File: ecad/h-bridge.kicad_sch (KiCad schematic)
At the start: 9 parts, among them Q1 40N06D, Q2 40N06D, U1 IR2104

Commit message: Use IRS2104
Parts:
- removed C2: C, symbol Device:C_Polarized
- added C2: C, Capacitor_SMD:C_0603_1608Metric, symbol Device:C
- D1: value D -> ES1D; footprint (none) -> Diode_SMD:D_SMA; LCSC Part # (none) -> C82648
- Q1, Q2: footprint Package_DFN_QFN:PQFN-8-EP_6x5mm_P1.27mm_Generic -> Package_TO_SOT_SMD:PQFN_8x8
- R1, R2: footprint (none) -> Resistor_SMD:R_0603_1608Metric
- U1: footprint (none) -> Package_SO:SOIC-8_3.9x4.9mm_P1.27mm
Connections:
- net OUT: now also C2.2
- net at D1.1 (K), U1.8 (VB): now also C2.1
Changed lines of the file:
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@@
 			)
 		)
-		(property "Footprint" ""
+		(property "Footprint" "Resistor_SMD:R_0603_1608Metric"
 			(at 153.67 108.458 90)
 			(effects
@@
 			)
 		)
-		(property "Footprint" "Package_DFN_QFN:PQFN-8-EP_6x5mm_P1.27mm_Generic"
+		(property "Footprint" "Package_TO_SOT_SMD:PQFN_8x8"
 			(at 170.18 91.44 0)
 			(effects
@@
 			)
 		)
-		(property "Footprint" "Package_DFN_QFN:PQFN-8-EP_6x5mm_P1.27mm_Generic"
+		(property "Footprint" "Package_TO_SOT_SMD:PQFN_8x8"
 			(at 170.18 104.14 0)
 			(effects
@@
 			)
 		)
-		(property "Footprint" ""
+		(property "Footprint" "Resistor_SMD:R_0603_1608Metric"
 			(at 153.67 95.758 90)
 			(effects
@@
 			)
 		)
-		(property "Footprint" ""
+		(property "Footprint" "Package_SO:SOIC-8_3.9x4.9mm_P1.27mm"
 			(at 121.92 99.06 0)
 			(effects
@@
 				(path "/192016dd-1af9-4f75-bd76-63c005f8be5e/9897782e-08fe-4e99-a389-7b164bfce6c4"
 					(reference "U1")
-					(unit 1)
-				)
-			)
-		)
-	)
-	(symbol
-		(lib_id "Device:C_Polarized")
-		(at 135.89 99.06 0)
-		(unit 1)
-		(exclude_from_sim no)
-		(in_bom yes)
-		(on_board yes)
-		(dnp no)
-		(fields_autoplaced yes)
-		(property "Reference" "C2"
-			(at 139.7 96.9009 0)
-			(effects
-				(font
-					(size 1.27 1.27)
-				)
-				(justify left)
-			)
-		)
-		(property "Value" "C"
-			(at 139.7 99.4409 0)
-			(effects
-				(font
-					(size 1.27 1.27)
-				)
-				(justify left)
-			)
-		)
-		(property "Footprint" ""
-			(at 136.8552 102.87 0)
-			(effects
-				(font
-					(size 1.27 1.27)
-				)
-				(hide yes)
-			)
-		)
-		(property "Datasheet" "~"
-			(at 135.89 99.06 0)
-			(effects
-				(font
-					(size 1.27 1.27)
-				)
-				(hide yes)
-			)
-		)
-		(property "Description" "Polarized capacitor"
-			(at 135.89 99.06 0)
-			(effects
-				(font
-					(size 1.27 1.27)
-				)
-				(hide yes)
-			)
-		)
-		(pin "2"
-		)
-		(pin "1"
-		)
-		(instances
-			(project ""
-				(path "/192016dd-1af9-4f75-bd76-63c005f8be5e/9897782e-08fe-4e99-a389-7b164bfce6c4"
-					(reference "C2")
 					(unit 1)
 				)
@@
 	)
 	(symbol
+		(lib_id "Device:C")
+		(at 135.89 99.06 0)
+		(unit 1)
+		(exclude_from_sim no)
+		(in_bom yes)
+		(on_board yes)
+		(dnp no)
+		(fields_autoplaced yes)
+		(property "Reference" "C2"
+			(at 139.7 97.7899 0)
+			(effects
+				(font
+					(size 1.27 1.27)
+				)
+				(justify left)
+			)
+		)
+		(property "Value" "C"
+			(at 139.7 100.3299 0)
+			(effects
+				(font
+					(size 1.27 1.27)
+				)
+				(justify left)
+			)
+		)
+		(property "Footprint" "Capacitor_SMD:C_0603_1608Metric"
+			(at 136.8552 102.87 0)
+			(effects
+				(font
+					(size 1.27 1.27)
+				)
+				(hide yes)
+			)
+		)
+		(property "Datasheet" "~"
+			(at 135.89 99.06 0)
+			(effects
+				(font
+					(size 1.27 1.27)
+				)
+				(hide yes)
+			)
+		)
+		(property "Description" "Unpolarized capacitor"
+			(at 135.89 99.06 0)
+			(effects
+				(font
+					(size 1.27 1.27)
+				)
+				(hide yes)
+			)
+		)
+		(pin "2"
+		)
+		(pin "1"
+		)
+		(instances
+			(project ""
+				(path "/192016dd-1af9-4f75-bd76-63c005f8be5e/9897782e-08fe-4e99-a389-7b164bfce6c4"
+					(reference "C2")
+					(unit 1)
+				)
+			)
+		)
+	)
+	(symbol
 		(lib_id "power:+12V")
 		(at 121.92 81.28 0)
@@
 			)
 		)
-		(property "Value" "D"
+		(property "Value" "ES1D"
 			(at 128.27 77.47 0)
 			(effects
@@
 			)
 		)
-		(property "Footprint" ""
+		(property "Footprint" "Diode_SMD:D_SMA"
 			(at 128.27 81.28 0)
 			(effects
@@
 			)
 		)
-		(property "Datasheet" "~"
+		(property "Datasheet" "https://www.lcsc.com/datasheet/lcsc_datasheet_1809291408_Vishay-Intertech-ES1D-E3-61T_C82648.pdf"
 			(at 128.27 81.28 0)
 			(effects
@@
 			(at 128.27 81.28 0)
 			(effects
+				(font
+					(size 1.27 1.27)
+				)
+				(hide yes)
+			)
+		)
+		(property "LCSC Part #" "C82648"
+			(at 128.27 81.28 0)
+			(effects

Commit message: Create PDFN-8-3x3 3d model
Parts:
- Q1, Q2: footprint Package_TO_SOT_SMD:PQFN_8x8 -> (none)
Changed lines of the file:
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@@
 			)
 		)
-		(property "Footprint" "Package_TO_SOT_SMD:PQFN_8x8"
+		(property "Footprint" ""
 			(at 170.18 91.44 0)
 			(effects
@@
 			)
 		)
-		(property "Footprint" "Package_TO_SOT_SMD:PQFN_8x8"
+		(property "Footprint" ""
 			(at 170.18 104.14 0)
 			(effects

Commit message: Work on MOSFET driver
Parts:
- removed C1: C, symbol Device:C_Polarized
- added C1: 470nF, Capacitor_SMD:C_0805_2012Metric, symbol Device:C
- added R3: 2.2, symbol Device:R
- C2: value C -> 47nF; LCSC Part # (none) -> C1622
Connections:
- net +12V: now also C1.1, R3.1; no longer D1.2 (A)
- net GND: now also C1.2
- new net: D1.2 (A), R3.2
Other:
- moved on the sheet: C2, C3, D1, Q1, Q2, R1, R2

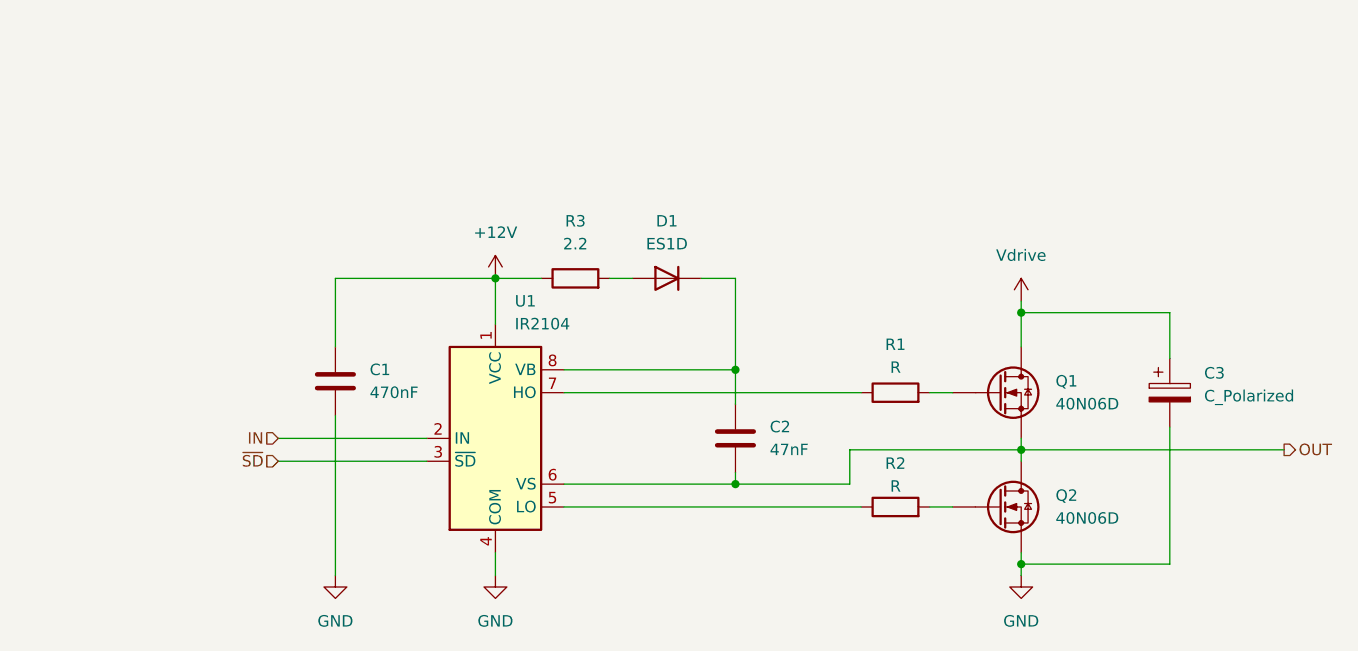
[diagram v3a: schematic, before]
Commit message: Initial half bridge layout
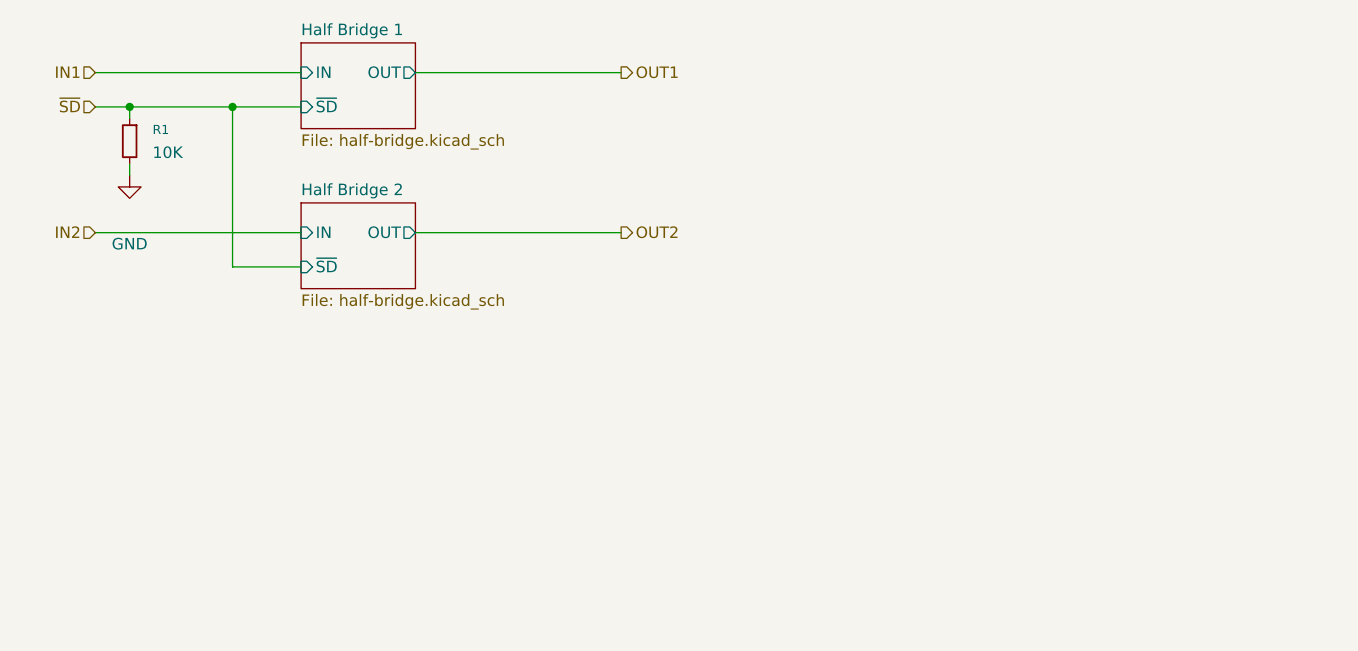
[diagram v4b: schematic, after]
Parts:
- removed C1: 470nF, Capacitor_SMD:C_0805_2012Metric, symbol Device:C
- removed C2: 47nF, Capacitor_SMD:C_0603_1608Metric, symbol Device:C
- removed C3: C_Polarized, symbol Device:C_Polarized
- removed D1: ES1D, Diode_SMD:D_SMA, symbol Device:D
- removed Q1, Q2: 40N06D, symbol Device:Q_NMOS
- removed R1, R2: R, Resistor_SMD:R_0603_1608Metric, symbol Device:R
- removed R3: 2.2, symbol Device:R
- removed U1: IR2104, Package_SO:SOIC-8_3.9x4.9mm_P1.27mm, symbol Driver_FET:IR2104
- added R1: 10K, Resistor_SMD:R_0603_1608Metric, symbol Device:R_Small
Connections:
- net GND: now also R1.2
- net ~{SD}: now also R1.1
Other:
- added sheet Half Bridge 1 (half-bridge.kicad_sch)
- added sheet Half Bridge 2 (half-bridge.kicad_sch)
